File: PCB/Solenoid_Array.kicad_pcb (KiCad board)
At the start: 2 copper layers, 750.7 x 332.5 mm, 112 parts, among them J1 Conn_01x02, J10 Conn_01x02, J11 Conn_01x02, J12 Conn_01x02, J13 Conn_01x02, J14 Conn_01x02, J15 Conn_01x02, J16 Power Daisy Chain_input, J17 Power Daisy Chain_Output, J18 Arduino Pins, J19 Screw_Terminal_01x02, J2 Conn_01x02, J3 Conn_01x02, J4 Conn_01x02, J5 Conn_01x02, J6 Conn_01x02, J7 Conn_01x02, J8 Conn_01x02, J9 Conn_01x02, Q1 AOD508, Q10 AOD508, Q11 AOD508, Q12 AOD508, Q13 AOD508, Q14 AOD508, Q15 AOD508, Q2 AOD508, Q3 AOD508, Q4 AOD508, Q5 AOD508, Q6 AOD508, Q7 AOD508, Q8 AOD508, Q9 AOD508

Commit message: Added silkscreen polarity and naming
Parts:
- D16, D17, D18, D19, D20, D21, D22, D23, D24, D25, D26, D27, D28, D29, D30: value IN-S126AT5UW -> LED IN-S126AT5UWr
- J19: footprint TerminalBlock_TE-Connectivity:TerminalBlock_TE_282834-2_1x02_P2.54mm_Horizontal -> troglodisme_footprints:TerminalBlock_TE_282834-2_1x02_P2.54mm_Horizontal
- Q1, Q10, Q11, Q12, Q13, Q14, Q15, Q2, Q3, Q4, Q5, Q6, Q7, Q8, Q9: value AOD508 -> TO252 (DPAK)
- R1, R10, R11, R12, R13, R14, R15, R16, R17, R18, R19, R2, R20, R21, R22, R23, R24, R25, R26, R27, R28, R29, R3, R30, R31, R32, R33, R34, R35, R36, R37, R38, R39, R4, R40, R41, R42, R43, R44, R45, R46, R5, R6, R7, R8, R9: footprint Resistor_SMD:R_1210_3225Metric_Pad1.42x2.65mm_HandSolder -> troglodisme_footprints:R_1210_3225Metric_Pad1.42x2.65mm_HandSolder
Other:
- board text added: "LETTERA AUTOMATA"
- board text added: "M3"

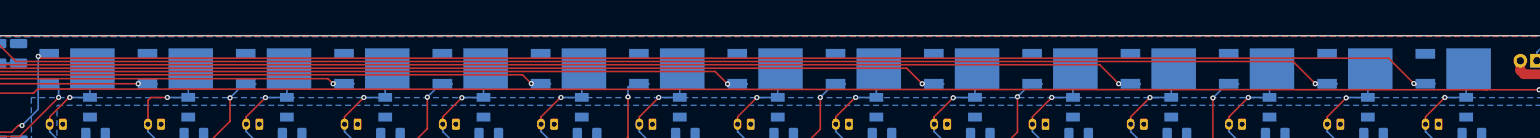
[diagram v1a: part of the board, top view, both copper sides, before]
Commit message: Repositioned Q1-15
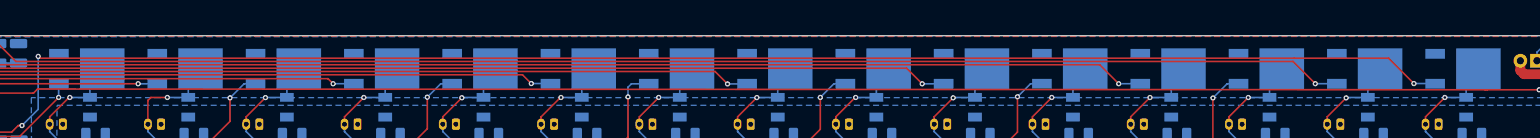
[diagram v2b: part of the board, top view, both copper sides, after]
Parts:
- J19: footprint troglodisme_footprints:TerminalBlock_TE_282834-2_1x02_P2.54mm_Horizontal -> TerminalBlock_TE-Connectivity:TerminalBlock_TE_282834-2_1x02_P2.54mm_Horizontal
- Q1, Q10, Q11, Q12, Q13, Q14, Q15, Q2, Q3, Q4, Q5, Q6, Q7, Q8, Q9: footprint troglodisme_footprints:AOD508 -> troglodisme_footprints:AOD508_GA
